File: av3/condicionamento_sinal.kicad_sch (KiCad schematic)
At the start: 20 parts, among them J10 Conn_01x03, J12 Conn_01x03, J13 Conn_01x03, J14 Conn_01x03, J15 Conn_02x04_Odd_Even, U6 TL084

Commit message: FEAT: Adição das footprints dos capacitores (C) e screw_terminals (J)
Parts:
- C10, C11: footprint (none) -> Capacitor_SMD:C_0805_2012Metric
- J10, J12, J13, J14: footprint (none) -> TerminalBlock_Phoenix:TerminalBlock_Phoenix_MKDS-1,5-3_1x03_P5.00mm_Horizontal
- J15, U6: footprint (none) -> Connector_PinHeader_2.54mm:PinHeader_2x04_P2.54mm_Vertical
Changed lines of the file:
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@@
 			)
 		)
-		(property "Footprint" ""
+		(property "Footprint" "Capacitor_SMD:C_0805_2012Metric"
 			(at 51.7652 119.38 0)
 			(effects
@@
 			)
 		)
-		(property "Footprint" ""
+		(property "Footprint" "TerminalBlock_Phoenix:TerminalBlock_Phoenix_MKDS-1,5-3_1x03_P5.00mm_Horizontal"
 			(at 152.4 63.5 0)
 			(effects
@@
 			)
 		)
-		(property "Footprint" ""
+		(property "Footprint" "Connector_PinHeader_2.54mm:PinHeader_2x04_P2.54mm_Vertical"
 			(at 133.35 66.04 0)
 			(effects
@@
 			)
 		)
-		(property "Footprint" ""
+		(property "Footprint" "Connector_PinHeader_2.54mm:PinHeader_2x04_P2.54mm_Vertical"
 			(at 133.35 90.17 0)
 			(effects
@@
 			)
 		)
-		(property "Footprint" ""
+		(property "Footprint" "Capacitor_SMD:C_0805_2012Metric"
 			(at 36.5252 119.38 0)
 			(effects
@@
 			)
 		)
-		(property "Footprint" ""
+		(property "Footprint" "Connector_PinHeader_2.54mm:PinHeader_2x04_P2.54mm_Vertical"
 			(at 40.64 85.09 0)
 			(effects
@@
 			)
 		)
-		(property "Footprint" ""
+		(property "Footprint" "Connector_PinHeader_2.54mm:PinHeader_2x04_P2.54mm_Vertical"
 			(at 133.35 137.16 0)
 			(effects
@@
 			)
 		)
-		(property "Footprint" ""
+		(property "Footprint" "TerminalBlock_Phoenix:TerminalBlock_Phoenix_MKDS-1,5-3_1x03_P5.00mm_Horizontal"
 			(at 152.4 134.62 0)
 			(effects
@@
 			)
 		)
-		(property "Footprint" ""
+		(property "Footprint" "Connector_PinHeader_2.54mm:PinHeader_2x04_P2.54mm_Vertical"
 			(at 133.35 114.3 0)
 			(effects
@@
 			)
 		)
-		(property "Footprint" ""
+		(property "Footprint" "TerminalBlock_Phoenix:TerminalBlock_Phoenix_MKDS-1,5-3_1x03_P5.00mm_Horizontal"
 			(at 152.4 87.63 0)
 			(effects
@@
 			)
 		)
-		(property "Footprint" ""
+		(property "Footprint" "Connector_PinHeader_2.54mm:PinHeader_2x04_P2.54mm_Vertical"
 			(at 40.64 110.49 0)
 			(effects
@@
 			)
 		)
-		(property "Footprint" ""
+		(property "Footprint" "TerminalBlock_Phoenix:TerminalBlock_Phoenix_MKDS-1,5-3_1x03_P5.00mm_Horizontal"
 			(at 152.4 111.76 0)
 			(effects

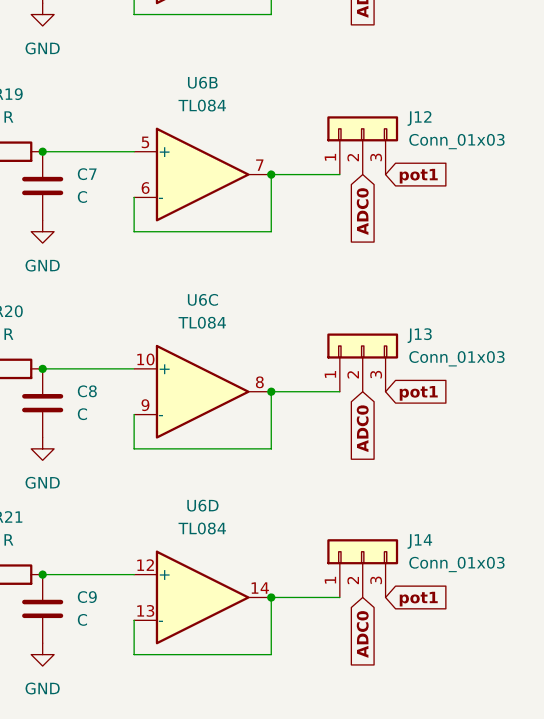
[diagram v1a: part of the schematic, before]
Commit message: Alteração do footprint do PS1 e inicio da PCB
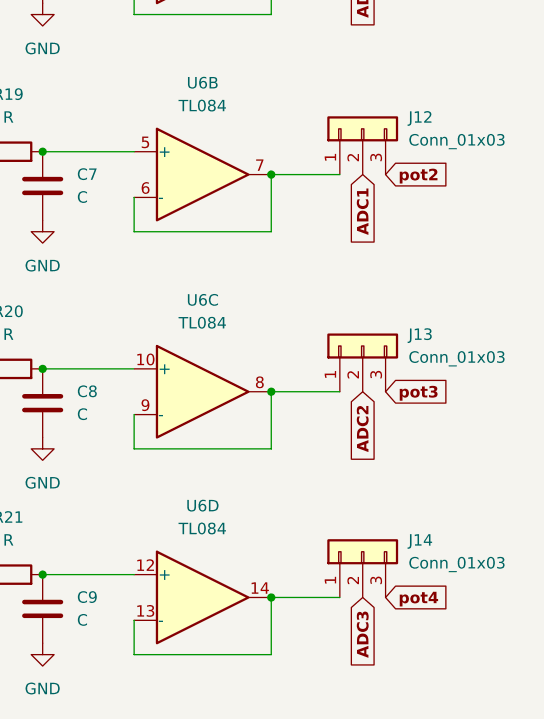
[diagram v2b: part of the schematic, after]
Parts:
- RV1, RV2, RV3, RV4: footprint (none) -> Resistor_THT:R_Axial_DIN0207_L6.3mm_D2.5mm_P7.62mm_Horizontal
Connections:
- net ADC0: no longer J12.2 (Pin_2), J13.2 (Pin_2), J14.2 (Pin_2)
- net pot1: no longer J12.3 (Pin_3), J13.3 (Pin_3), J14.3 (Pin_3)
- net pot2: now also J12.3 (Pin_3)
- net pot3: now also J13.3 (Pin_3)
- net pot4: now also J14.3 (Pin_3)
- new net ADC1: J12.2 (Pin_2)
- new net ADC2: J13.2 (Pin_2)
- new net ADC3: J14.2 (Pin_2)
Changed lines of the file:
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@@
 		)
 	)
-	(global_label "pot1"
+	(global_label "pot3"
 		(shape input)
 		(at 154.94 116.84 0)
@@
 		)
 	)
-	(global_label "ADC0"
+	(global_label "ADC1"
 		(shape input)
 		(at 152.4 92.71 270)
@@
 		)
 	)
-	(global_label "pot1"
+	(global_label "pot2"
 		(shape input)
 		(at 154.94 92.71 0)
@@
 		)
 	)
-	(global_label "ADC0"
+	(global_label "ADC3"
 		(shape input)
 		(at 152.4 139.7 270)
@@
 		)
 	)
-	(global_label "pot1"
+	(global_label "pot4"
 		(shape input)
 		(at 154.94 139.7 0)
@@
 		)
 	)
-	(global_label "ADC0"
+	(global_label "ADC2"
 		(shape input)
 		(at 152.4 116.84 270)
@@
 			)
 		)
-		(property "Footprint" ""
+		(property "Footprint" "Resistor_THT:R_Axial_DIN0207_L6.3mm_D2.5mm_P7.62mm_Horizontal"
 			(at 77.47 88.9 0)
 			(effects
@@
 			)
 		)
-		(property "Footprint" ""
+		(property "Footprint" "Resistor_THT:R_Axial_DIN0207_L6.3mm_D2.5mm_P7.62mm_Horizontal"
 			(at 77.47 110.49 0)
 			(effects
@@
 			)
 		)
-		(property "Footprint" ""
+		(property "Footprint" "Resistor_THT:R_Axial_DIN0207_L6.3mm_D2.5mm_P7.62mm_Horizontal"
 			(at 77.47 67.31 0)
 			(effects
@@
 			)
 		)
-		(property "Footprint" ""
+		(property "Footprint" "Resistor_THT:R_Axial_DIN0207_L6.3mm_D2.5mm_P7.62mm_Horizontal"
 			(at 77.47 132.08 0)
 			(effects

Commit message: Mudança de footprints e mudança na PCB
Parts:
- J10, J12, J13, J14: footprint TerminalBlock_Phoenix:TerminalBlock_Phoenix_MKDS-1,5-3_1x03_P5.00mm_Horizontal -> Connector_PinHeader_2.54mm:PinHeader_1x03_P2.54mm_Vertical
- J15: footprint Connector_PinHeader_2.54mm:PinHeader_2x04_P2.54mm_Vertical -> Connector_IDC:IDC-Header_2x04_P2.54mm_Vertical
- R18, R19, R20, R21: value R -> 10K; footprint (none) -> Resistor_THT:R_Axial_DIN0207_L6.3mm_D2.5mm_P7.62mm_Horizontal
- RV1, RV2, RV3, RV4: footprint Resistor_THT:R_Axial_DIN0207_L6.3mm_D2.5mm_P7.62mm_Horizontal -> Potentiometer_THT:Potentiometer_Bourns_3296W_Vertical
- U6: footprint Connector_PinHeader_2.54mm:PinHeader_2x04_P2.54mm_Vertical -> Package_DIP:DIP-14_W7.62mm
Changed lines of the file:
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@@
 			)
 		)
-		(property "Footprint" "TerminalBlock_Phoenix:TerminalBlock_Phoenix_MKDS-1,5-3_1x03_P5.00mm_Horizontal"
+		(property "Footprint" "Connector_PinHeader_2.54mm:PinHeader_1x03_P2.54mm_Vertical"
 			(at 152.4 63.5 0)
 			(effects
@@
 			)
 		)
-		(property "Value" "R"
+		(property "Value" "10K"
 			(at 113.03 110.49 90)
 			(effects
@@
 			)
 		)
-		(property "Footprint" ""
+		(property "Footprint" "Resistor_THT:R_Axial_DIN0207_L6.3mm_D2.5mm_P7.62mm_Horizontal"
 			(at 113.03 116.078 90)
 			(effects
@@
 			)
 		)
-		(property "Value" "R"
+		(property "Value" "10K"
 			(at 113.03 62.23 90)
 			(effects
@@
 			)
 		)
-		(property "Footprint" ""
+		(property "Footprint" "Resistor_THT:R_Axial_DIN0207_L6.3mm_D2.5mm_P7.62mm_Horizontal"
 			(at 113.03 67.818 90)
 			(effects
@@
 			)
 		)
-		(property "Footprint" "Connector_PinHeader_2.54mm:PinHeader_2x04_P2.54mm_Vertical"
+		(property "Footprint" "Package_DIP:DIP-14_W7.62mm"
 			(at 133.35 66.04 0)
 			(effects
@@
 			)
 		)
-		(property "Footprint" "Connector_PinHeader_2.54mm:PinHeader_2x04_P2.54mm_Vertical"
+		(property "Footprint" "Package_DIP:DIP-14_W7.62mm"
 			(at 133.35 90.17 0)
 			(effects
@@
 			)
 		)
-		(property "Footprint" "Connector_PinHeader_2.54mm:PinHeader_2x04_P2.54mm_Vertical"
+		(property "Footprint" "Connector_IDC:IDC-Header_2x04_P2.54mm_Vertical"
 			(at 40.64 85.09 0)
 			(effects
@@
 			)
 		)
-		(property "Footprint" "Resistor_THT:R_Axial_DIN0207_L6.3mm_D2.5mm_P7.62mm_Horizontal"
+		(property "Footprint" "Potentiometer_THT:Potentiometer_Bourns_3296W_Vertical"
 			(at 77.47 88.9 0)
 			(effects
@@
 			)
 		)
-		(property "Footprint" "Connector_PinHeader_2.54mm:PinHeader_2x04_P2.54mm_Vertical"
+		(property "Footprint" "Package_DIP:DIP-14_W7.62mm"
 			(at 133.35 137.16 0)
 			(effects
@@
 			)
 		)
-		(property "Value" "R"
+		(property "Value" "10K"
 			(at 113.03 86.36 90)
 			(effects
@@
 			)
 		)
-		(property "Footprint" ""
+		(property "Footprint" "Resistor_THT:R_Axial_DIN0207_L6.3mm_D2.5mm_P7.62mm_Horizontal"
 			(at 113.03 91.948 90)
 			(effects
@@
 			)
 		)
-		(property "Footprint" "TerminalBlock_Phoenix:TerminalBlock_Phoenix_MKDS-1,5-3_1x03_P5.00mm_Horizontal"
+		(property "Footprint" "Connector_PinHeader_2.54mm:PinHeader_1x03_P2.54mm_Vertical"
 			(at 152.4 134.62 0)
 			(effects
@@
 			)
 		)
-		(property "Footprint" "Connector_PinHeader_2.54mm:PinHeader_2x04_P2.54mm_Vertical"
+		(property "Footprint" "Package_DIP:DIP-14_W7.62mm"
 			(at 133.35 114.3 0)
 			(effects
@@
 			)
 		)
-		(property "Value" "R"
+		(property "Value" "10K"
 			(at 113.03 133.35 90)
 			(effects
@@
 			)
 		)
-		(property "Footprint" ""
+		(property "Footprint" "Resistor_THT:R_Axial_DIN0207_L6.3mm_D2.5mm_P7.62mm_Horizontal"
 			(at 113.03 138.938 90)
 			(effects
@@
 			)
 		)
-		(property "Footprint" "Resistor_THT:R_Axial_DIN0207_L6.3mm_D2.5mm_P7.62mm_Horizontal"
+		(property "Footprint" "Potentiometer_THT:Potentiometer_Bourns_3296W_Vertical"
 			(at 77.47 110.49 0)
 			(effects
@@
 			)
 		)
-		(property "Footprint" "Resistor_THT:R_Axial_DIN0207_L6.3mm_D2.5mm_P7.62mm_Horizontal"
+		(property "Footprint" "Potentiometer_THT:Potentiometer_Bourns_3296W_Vertical"
 			(at 77.47 67.31 0)
 			(effects
@@
 			)
 		)
-		(property "Footprint" "TerminalBlock_Phoenix:TerminalBlock_Phoenix_MKDS-1,5-3_1x03_P5.00mm_Horizontal"
+		(property "Footprint" "Connector_PinHeader_2.54mm:PinHeader_1x03_P2.54mm_Vertical"
 			(at 152.4 87.63 0)
 			(effects
@@
 			)
 		)
-		(property "Footprint" "Resistor_THT:R_Axial_DIN0207_L6.3mm_D2.5mm_P7.62mm_Horizontal"
+		(property "Footprint" "Potentiometer_THT:Potentiometer_Bourns_3296W_Vertical"
 			(at 77.47 132.08 0)
 			(effects
@@
 			)
 		)
-		(property "Footprint" "Connector_PinHeader_2.54mm:PinHeader_2x04_P2.54mm_Vertical"
+		(property "Footprint" "Package_DIP:DIP-14_W7.62mm"
 			(at 40.64 110.49 0)
 			(effects
@@
 			)
 		)
-		(property "Footprint" "TerminalBlock_Phoenix:TerminalBlock_Phoenix_MKDS-1,5-3_1x03_P5.00mm_Horizontal"
+		(property "Footprint" "Connector_PinHeader_2.54mm:PinHeader_1x03_P2.54mm_Vertical"
 			(at 152.4 111.76 0)
 			(effects

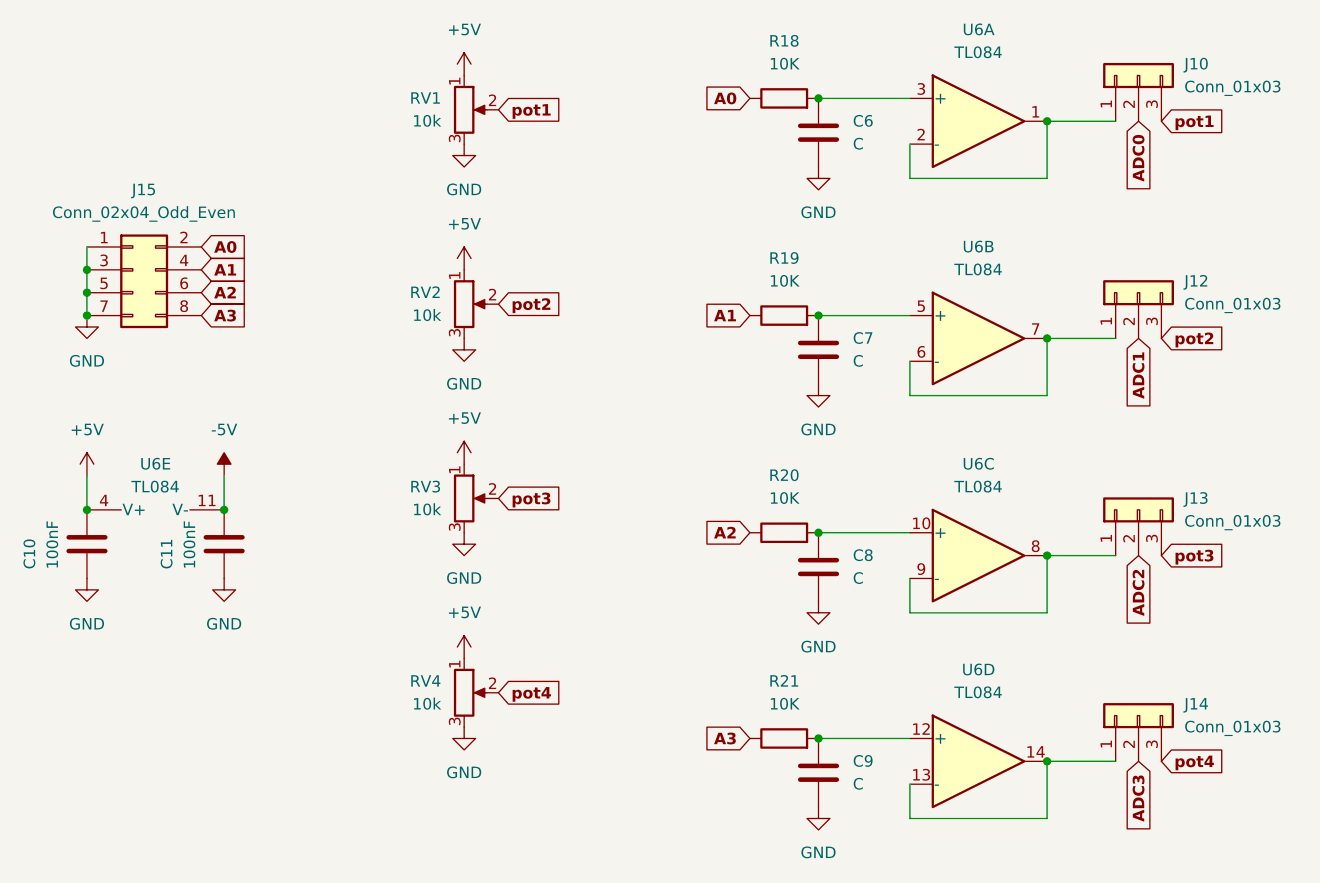
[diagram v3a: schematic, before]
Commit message: Algumas trilhas feitas
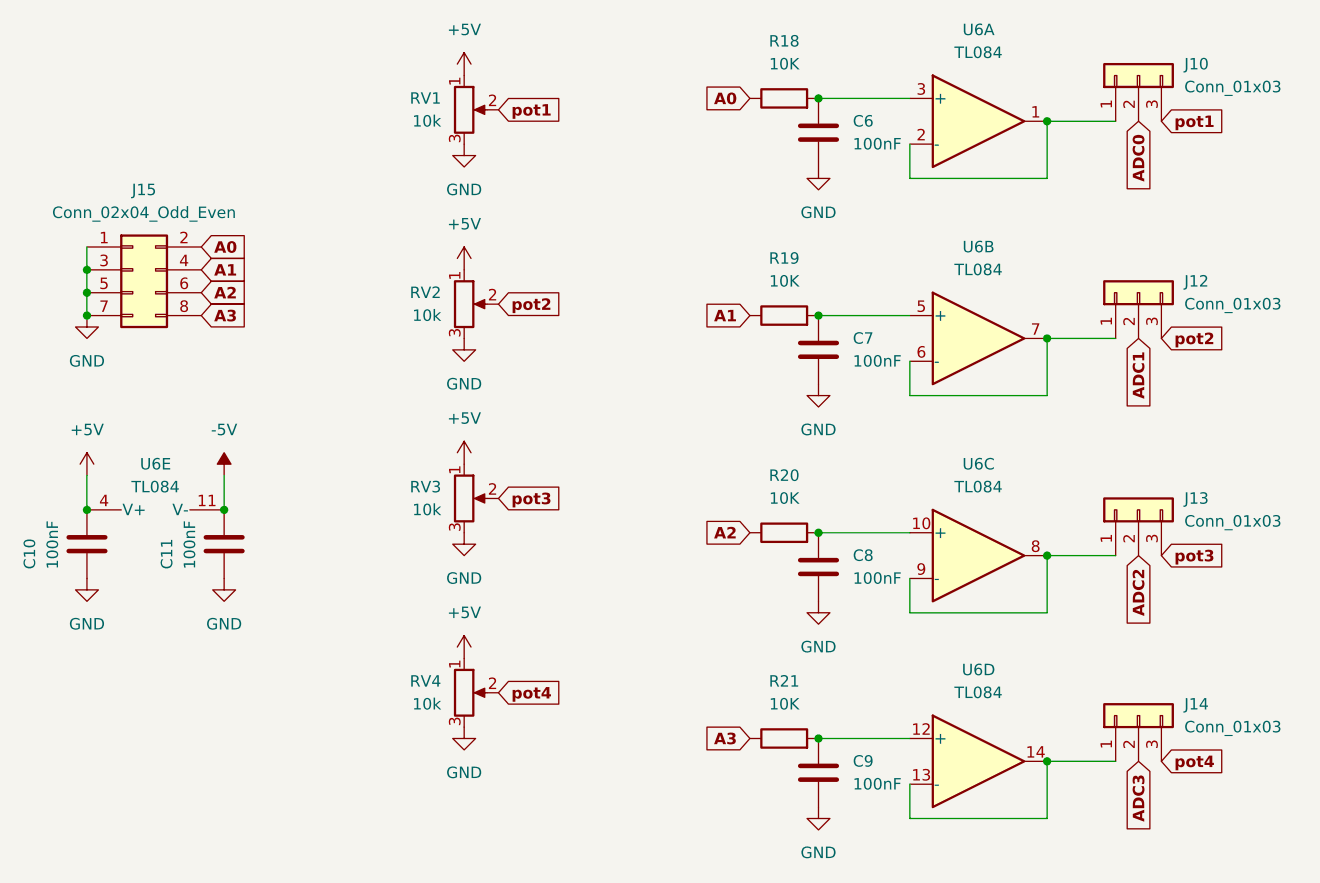
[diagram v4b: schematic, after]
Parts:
- C6, C7, C8, C9: value C -> 100nF; footprint (none) -> Capacitor_THT:CP_Radial_D4.0mm_P1.50mm
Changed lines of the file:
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@@
 			)
 		)
-		(property "Value" "C"
+		(property "Value" "100nF"
 			(at 120.65 95.2499 0)
 			(effects
@@
 			)
 		)
-		(property "Footprint" ""
+		(property "Footprint" "Capacitor_THT:CP_Radial_D4.0mm_P1.50mm"
 			(at 117.8052 97.79 0)
 			(effects
@@
 			)
 		)
-		(property "Value" "C"
+		(property "Value" "100nF"
 			(at 120.65 119.3799 0)
 			(effects
@@
 			)
 		)
-		(property "Footprint" ""
+		(property "Footprint" "Capacitor_THT:CP_Radial_D4.0mm_P1.50mm"
 			(at 117.8052 121.92 0)
 			(effects
@@
 			)
 		)
-		(property "Value" "C"
+		(property "Value" "100nF"
 			(at 120.65 142.2399 0)
 			(effects
@@
 			)
 		)
-		(property "Footprint" ""
+		(property "Footprint" "Capacitor_THT:CP_Radial_D4.0mm_P1.50mm"
 			(at 117.8052 144.78 0)
 			(effects
@@
 			)
 		)
-		(property "Value" "C"
+		(property "Value" "100nF"
 			(at 120.65 71.1199 0)
 			(effects
@@
 			)
 		)
-		(property "Footprint" ""
+		(property "Footprint" "Capacitor_THT:CP_Radial_D4.0mm_P1.50mm"
 			(at 117.8052 73.66 0)
 			(effects

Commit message: Finaliza a organização dos componentes na PCB, ajusta footprints
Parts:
- C6, C7, C8, C9: footprint Capacitor_THT:CP_Radial_D4.0mm_P1.50mm -> Capacitor_SMD:C_0805_2012Metric
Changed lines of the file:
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@@
 			)
 		)
-		(property "Footprint" "Capacitor_THT:CP_Radial_D4.0mm_P1.50mm"
+		(property "Footprint" "Capacitor_SMD:C_0805_2012Metric"
 			(at 117.8052 97.79 0)
 			(effects
@@
 			)
 		)
-		(property "Footprint" "Capacitor_THT:CP_Radial_D4.0mm_P1.50mm"
+		(property "Footprint" "Capacitor_SMD:C_0805_2012Metric"
 			(at 117.8052 121.92 0)
 			(effects
@@
 			)
 		)
-		(property "Footprint" "Capacitor_THT:CP_Radial_D4.0mm_P1.50mm"
+		(property "Footprint" "Capacitor_SMD:C_0805_2012Metric"
 			(at 117.8052 144.78 0)
 			(effects
@@
 			)
 		)
-		(property "Footprint" "Capacitor_THT:CP_Radial_D4.0mm_P1.50mm"
+		(property "Footprint" "Capacitor_SMD:C_0805_2012Metric"
 			(at 117.8052 73.66 0)
 			(effects
